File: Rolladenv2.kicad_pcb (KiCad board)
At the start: 4 copper layers, 108.7 x 73.7 mm, 9 parts, among them U1 ESP32-S3, Y1 50MHz

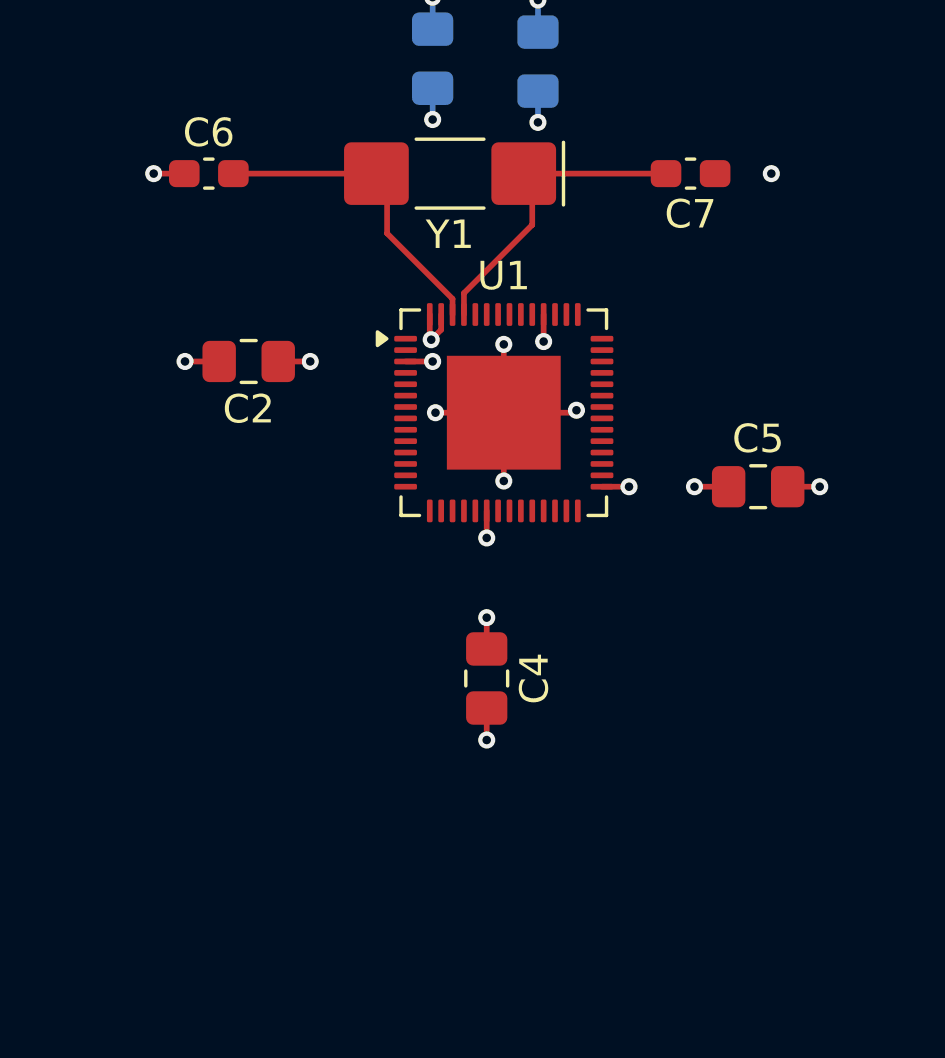
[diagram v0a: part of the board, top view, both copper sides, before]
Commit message: Added Reset Circuitry
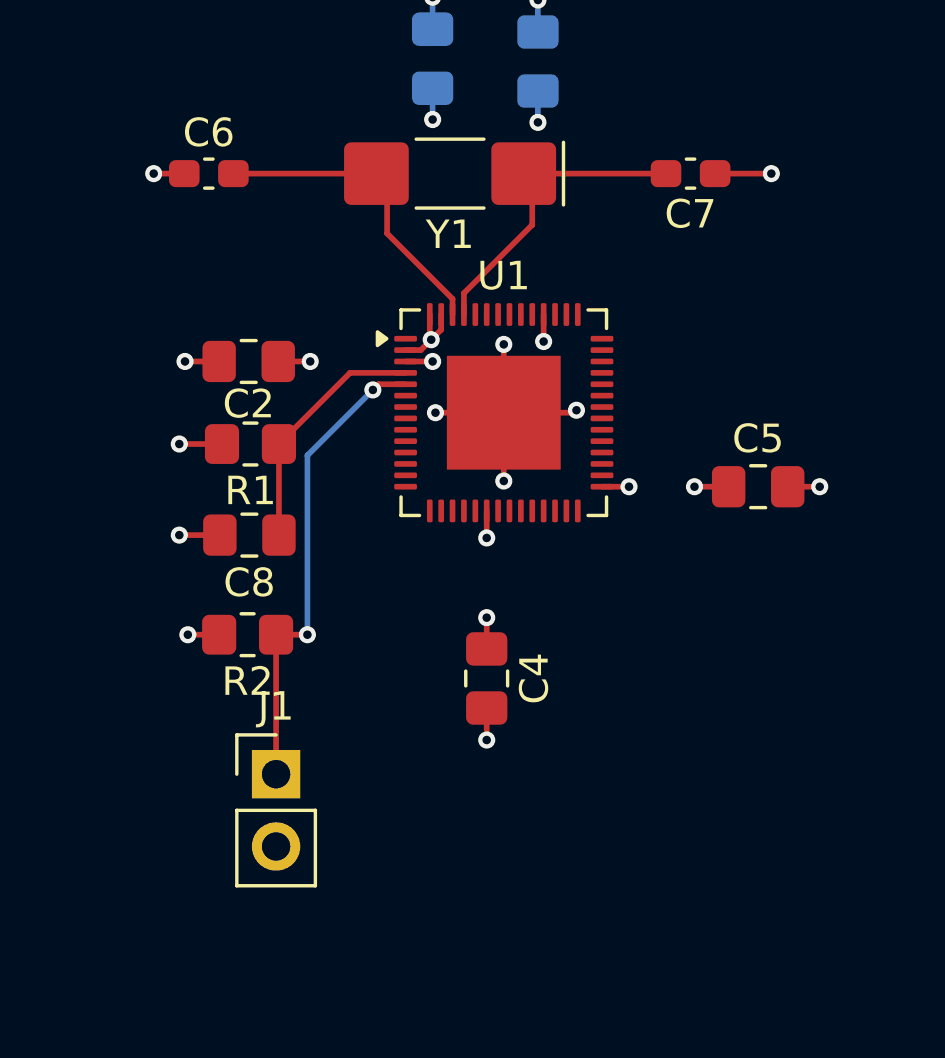
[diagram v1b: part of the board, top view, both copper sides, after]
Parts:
- added C8: 0.1µF, Capacitor_SMD:C_0805_2012Metric_Pad1.18x1.45mm_HandSolder, F.Cu at (67.9, 49.0)
- added J1: Conn_01x02_Pin, Connector_PinHeader_2.54mm:PinHeader_1x02_P2.54mm_Vertical, F.Cu at (68.8, 57.4)
- added R1: 10kΩ, Resistor_SMD:R_0805_2012Metric_Pad1.20x1.40mm_HandSolder, F.Cu at (67.9, 45.8)
- added R2: 10kΩ, Resistor_SMD:R_0805_2012Metric_Pad1.20x1.40mm_HandSolder, F.Cu at (67.8, 52.5)
- C6, C7: value C -> 12pF
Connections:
- net Net-(U1-XTAL_N) renamed XTAL_N
- net Net-(U1-XTAL_P) renamed XTAL_P
- U1 pad 4: unconnected-(U1-CHIP_PU-Pad4) -> RESET
- U1 pad 5: unconnected-(U1-GPIO0-Pad5) -> BOOTSEL
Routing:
- net BOOTSEL: track 0.00 -> 16.8 mm, vias 0 -> 2
- net RESET: track 0.00 -> 8.69 mm
- net VDD: track 11.4 -> 15.0 mm, vias 10 -> 12
- net GND: track 16.6 -> 20.0 mm, vias 11 -> 12

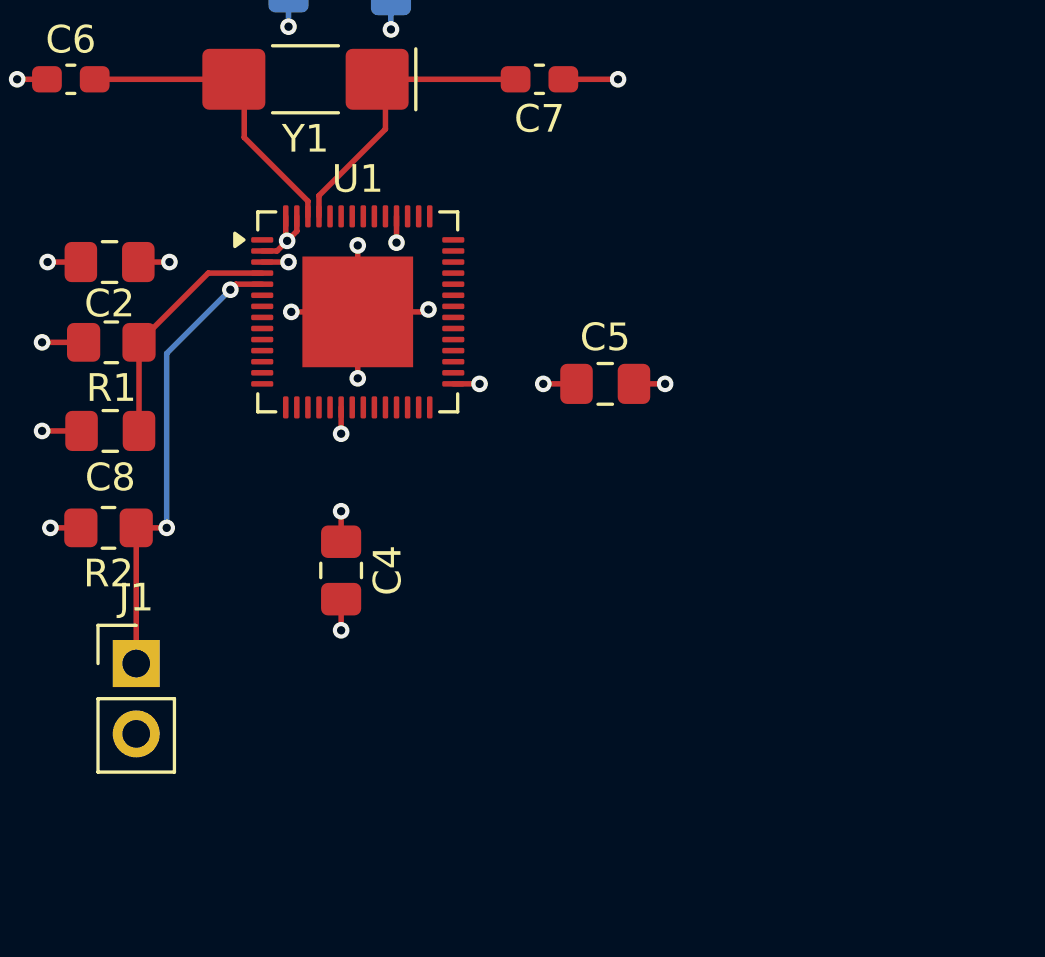
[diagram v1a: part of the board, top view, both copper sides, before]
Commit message: Added Flash Data
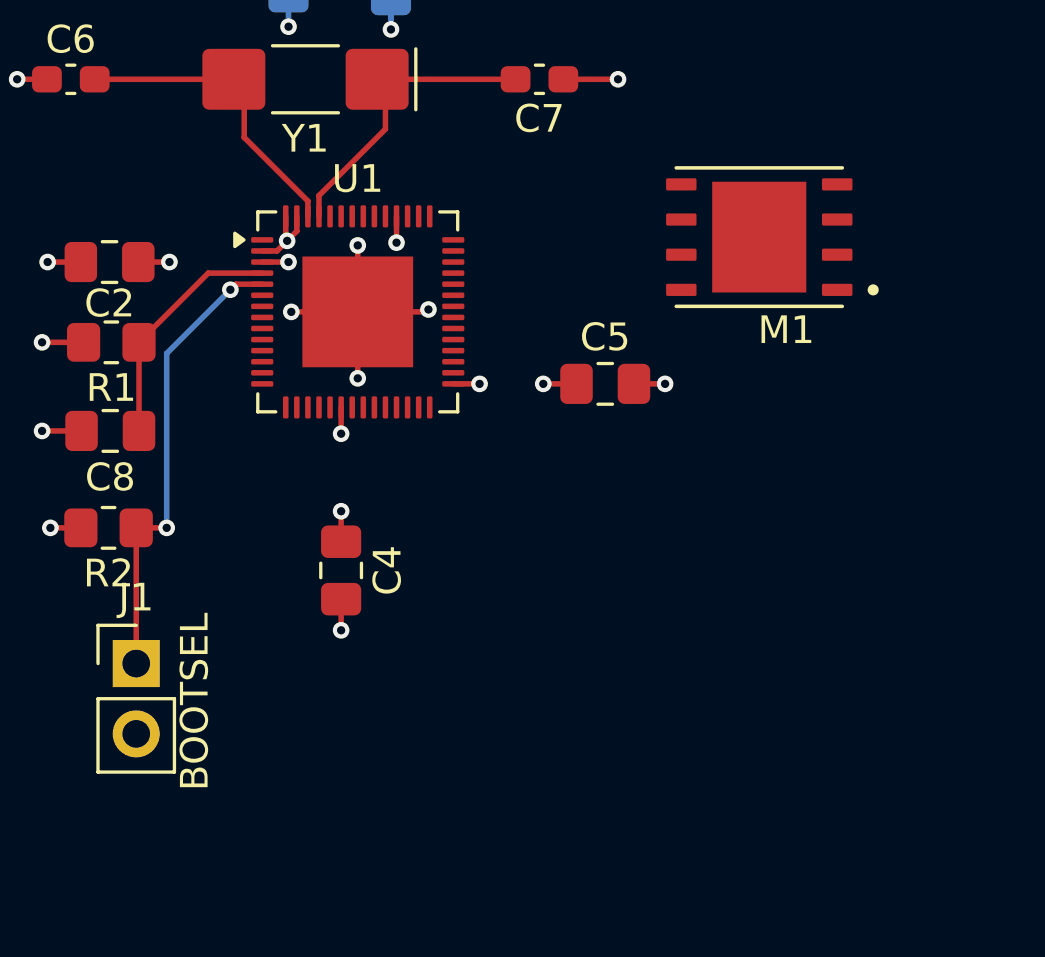
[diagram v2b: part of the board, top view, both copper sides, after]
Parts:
- added M1: ~, AT25SL641-MHE-T:SON127P500X600X60-9N, F.Cu at (91.3, 42.0)
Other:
- board text added: "BOOTSEL"
